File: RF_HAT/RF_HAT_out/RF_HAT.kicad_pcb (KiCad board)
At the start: 8 copper layers, 56 x 65 mm, 83 parts, among them J1 SMA, J2 SMA, J3 Raspberry_Pi_2_3, U1 CC1200RHBR, U2 CC1200RHBR, U3 RaspberryPi_Pico, Y1 40MHz, Y2 40MHz

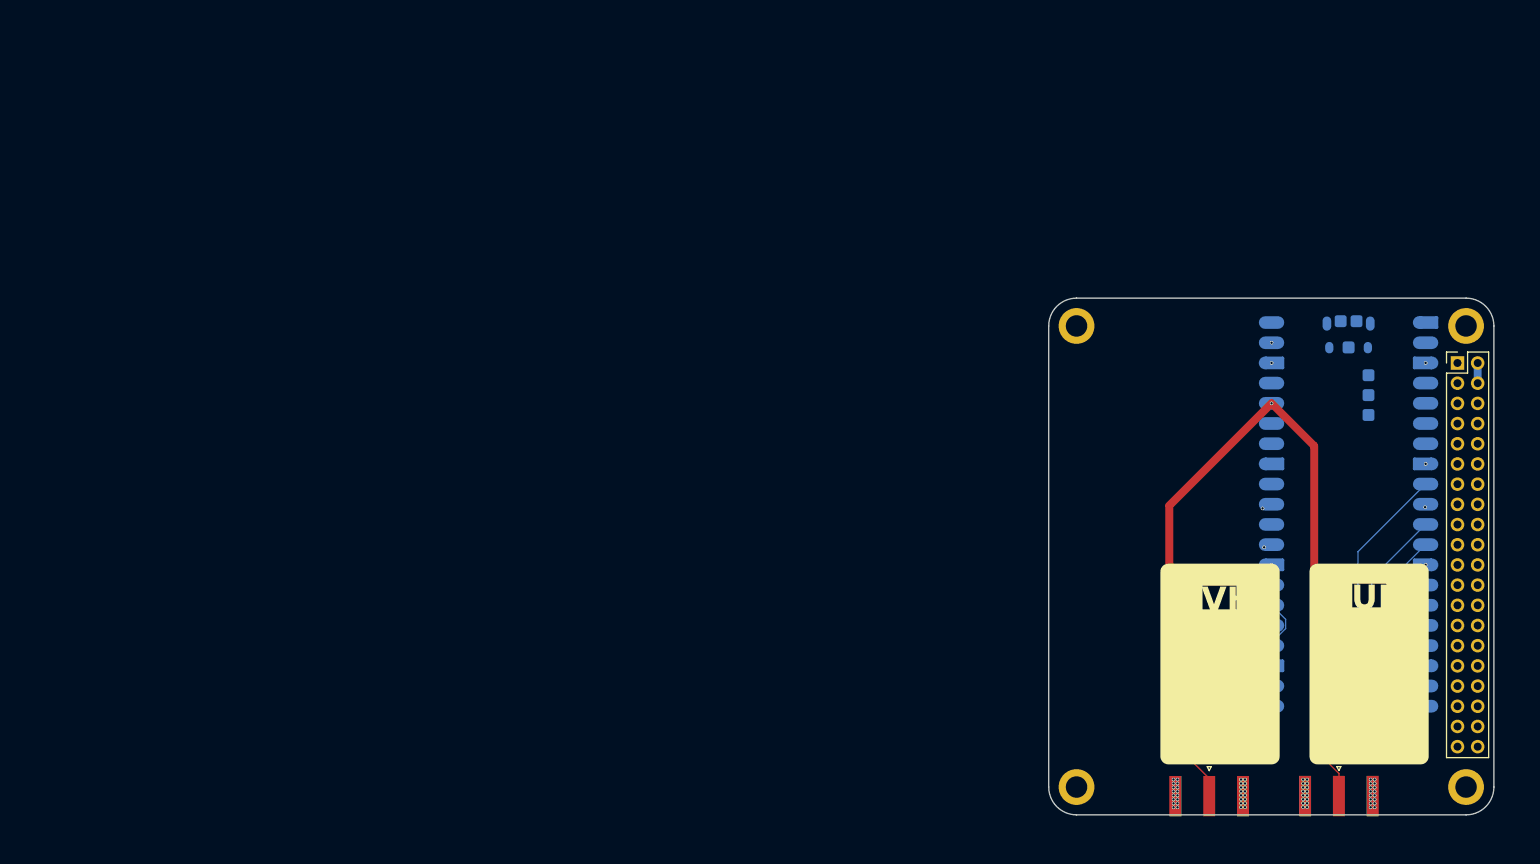
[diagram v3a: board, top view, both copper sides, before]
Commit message: Restructured kicad schematic for CC1200 PI_HAT readablitity based on M17 reference schematics
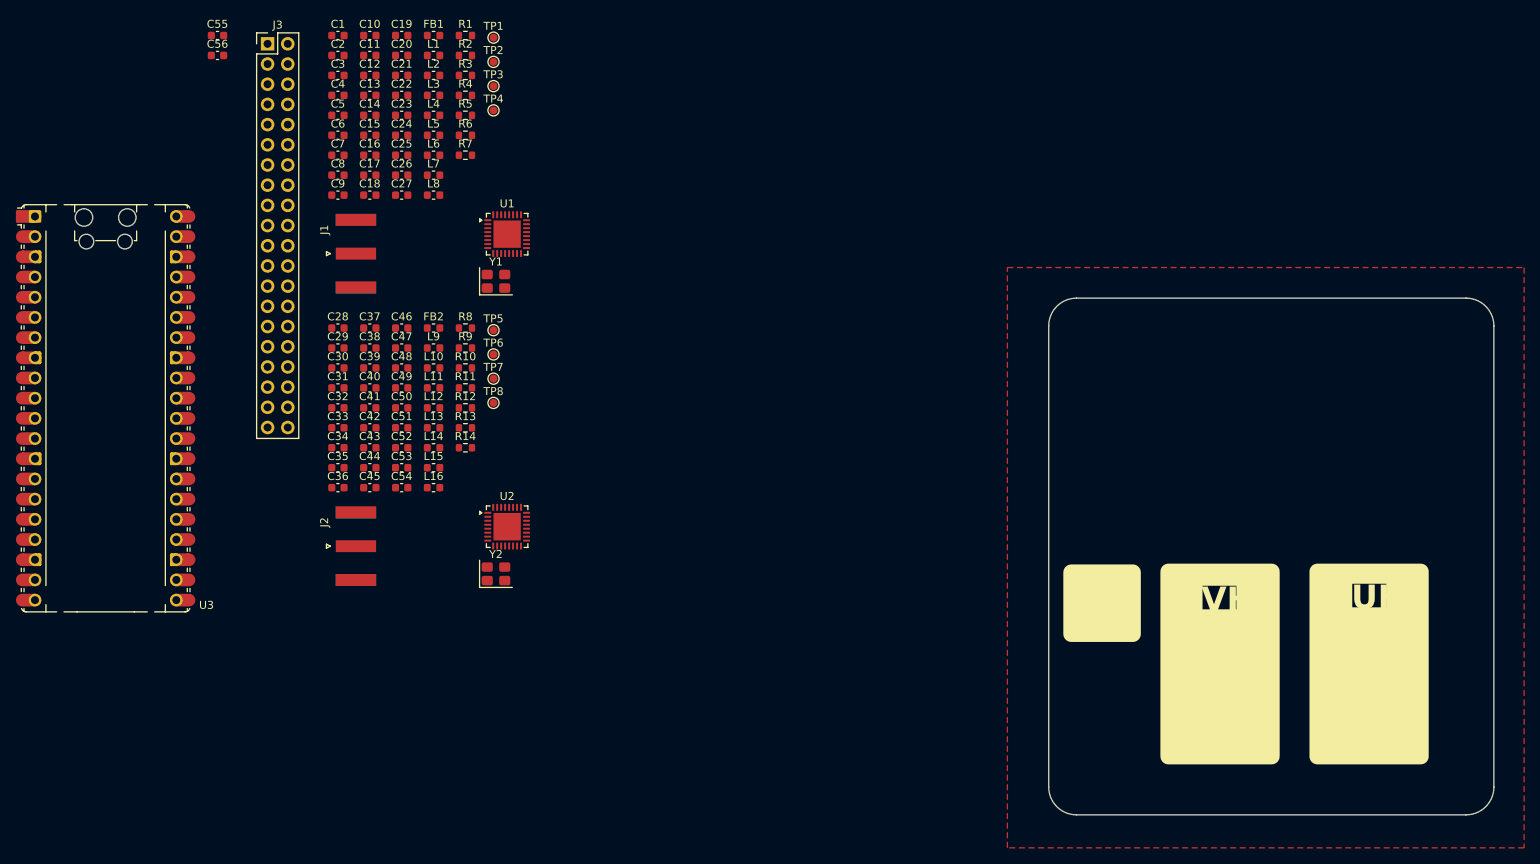
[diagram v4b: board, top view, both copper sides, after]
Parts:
- removed H1, H2, H3, H4: MountingHole_Pad, MountingHole:MountingHole_2.7mm_M2.5_ISO14580_Pad
- added C51: 47nF, Capacitor_SMD:C_0603_1608Metric, F.Cu at (80.8, 77.2)
- added C52: 47nF, Capacitor_SMD:C_0603_1608Metric, F.Cu at (80.8, 79.7)
- added C53: 47nF, Capacitor_SMD:C_0603_1608Metric, F.Cu at (80.8, 82.2)
- added C54: 47nF, Capacitor_SMD:C_0603_1608Metric, F.Cu at (80.8, 84.7)
- added C55: 100nF, Capacitor_SMD:C_0603_1608Metric, F.Cu at (57.6, 27.8)
- added C56: 100nF, Capacitor_SMD:C_0603_1608Metric, F.Cu at (57.6, 30.3)
- added L16: 100nH, Inductor_SMD:L_0603_1608Metric, F.Cu at (84.8, 84.7)
- added R10: 100R, Resistor_SMD:R_0603_1608Metric, F.Cu at (88.8, 69.6)
- added R11: 10k, Resistor_SMD:R_0603_1608Metric, F.Cu at (88.8, 72.1)
- added R12: 10k, Resistor_SMD:R_0603_1608Metric, F.Cu at (88.8, 74.7)
- added R13: 22R, Resistor_SMD:R_0603_1608Metric, F.Cu at (88.8, 77.2)
- added R14: 56k, Resistor_SMD:R_0603_1608Metric, F.Cu at (88.8, 79.7)
- added R5: 10k, Resistor_SMD:R_0603_1608Metric, F.Cu at (88.8, 37.9)
- added R6: 18R, Resistor_SMD:R_0603_1608Metric, F.Cu at (88.8, 40.4)
- added R7: 56k, Resistor_SMD:R_0603_1608Metric, F.Cu at (88.8, 42.9)
- added R8: 100R, Resistor_SMD:R_0603_1608Metric, F.Cu at (88.8, 64.6)
- added R9: 100R, Resistor_SMD:R_0603_1608Metric, F.Cu at (88.8, 67.1)
- added TP1: ~, TestPoint:TestPoint_Pad_D1.0mm, F.Cu at (92.4, 28.1)
- added TP2: ~, TestPoint:TestPoint_Pad_D1.0mm, F.Cu at (92.4, 31.1)
- added TP3: ~, TestPoint:TestPoint_Pad_D1.0mm, F.Cu at (92.4, 34.2)
- added TP4: ~, TestPoint:TestPoint_Pad_D1.0mm, F.Cu at (92.4, 37.2)
- added TP5: ~, TestPoint:TestPoint_Pad_D1.0mm, F.Cu at (92.4, 64.9)
- added TP6: ~, TestPoint:TestPoint_Pad_D1.0mm, F.Cu at (92.4, 67.9)
- added TP7: ~, TestPoint:TestPoint_Pad_D1.0mm, F.Cu at (92.4, 71.0)
- added TP8: ~, TestPoint:TestPoint_Pad_D1.0mm, F.Cu at (92.4, 74.0)
- C1: value 15pF -> 2.2pF
- C10: value 47nF -> 1nF
- C11, C38: value 47nF -> 10nF
- C12, C13, C35, C36, C39, C40: value 47nF -> 15pF
- C14, C15, C16, C41: value 47nF -> 100nF
- C17, C42: value 10nF -> 100nF
- C18: value 5.1pF -> 1.5nF
- C19: value 56pF -> 220nF
- C2: value 15pF -> 39pF
- C20: value 100pF -> 10nF
- C21: value 39pF -> 47nF
- C22, C25: value 5.1pF -> 47nF
- C23: value 6.2pF -> 47nF
- C24: value 2.2pF -> 47nF
- C26, C27, C48, C49: value 15pF -> 47nF
- C28: value 100nF -> 1.5pF
- C29: value 100nF -> 100pF
- C3: value 100nF -> 5.1pF
- C30, C31: value 100nF -> 15pF
- C32: value 1.8nF -> 100pF
- C33: value 220nF -> 10nF
- C34: value 10nF -> 100pF
- C37: value 47nF -> 100pF
- C4: value 100nF -> 6.2pF
- C43, C44: value 100pF -> 100nF
- C45: value 15pF -> 1.8nF
- C46: value 1.5pF -> 220nF
- C47: value 15pF -> 10nF
- C5: value 100nF -> 56pF
- C50: value 100pF -> 47nF
- C6: value 100nF -> 10nF
- C7: value 1.5nF -> 100pF
- C8: value 220nF -> 5.1pF
- C9: value 10nF -> 5.1pF
- L1: value 56nH -> 15nH
- L10: value 22nH -> 120nH
- L11: value 120nH -> 82nH
- L12: value 82nH -> 270nH
- L13: value 180nH -> 47nH
- L15: value 47nH -> 180nH
- L2: value 56nH -> 43nH
- L3: value 27nH -> 22nH
- L4: value 27nH -> 56nH
- L6: value 43nH -> 27nH
- L7: value 22nH -> 56nH
- L8: value 15nH -> 27nH
- L9: value 270nH -> 22nH
- R1, R3: value 56k -> 100R
- R2: value 18R -> 100R
- R4: value 22R -> 10k
- U3: footprint Module:RaspberryPi_Pico_SMD -> Module:RaspberryPi_Pico_Common_Unspecified; moved to F.Cu
- moved U3 156.9 mm to (43.6, 74.7), turned to 0 degrees
- moved C1 155.4 mm to (72.8, 27.8), turned to 0 degrees
- moved J3 155.0 mm to (63.9, 28.9)
- moved C10 153.9 mm to (76.8, 27.8)
- moved C5 153.1 mm to (72.8, 37.9)
- moved C19 151.8 mm to (80.8, 27.8), turned to 0 degrees
- moved C21 151.5 mm to (80.8, 32.8), turned to 0 degrees
- moved C20 151.5 mm to (80.8, 30.3)
- moved C2 150.5 mm to (72.8, 30.3)
- moved C6 150.0 mm to (72.8, 40.4)
- moved C4 149.4 mm to (72.8, 35.3), turned to 0 degrees
- moved C22 148.7 mm to (80.8, 35.3), turned to 0 degrees
- moved C7 148.6 mm to (72.8, 42.9), turned to 0 degrees
- moved C16 147.9 mm to (76.8, 42.9)
- moved C9 147.5 mm to (72.8, 47.9)
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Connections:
- C1 pad 1: /CC1200_UHF_432MHz/UHF_XOSC_Q1 -> /CC1200_UHF_432MHz/UHF_MN1
- C1 pad 2: /GND -> /CC1200_UHF_432MHz/UHF_MN2
- C10 pad 1: /CC1200_UHF_432MHz/UHF_AVDD_FILT -> /CC1200_UHF_432MHz/UHF_ANT_PRE
- C10 pad 2: /GND -> /CC1200_UHF_432MHz/UHF_ANT
- C12 pad 1: /CC1200_UHF_432MHz/UHF_AVDD_FILT -> /CC1200_UHF_432MHz/UHF_XOSC_Q1
- C13 pad 1: /CC1200_UHF_432MHz/UHF_AVDD_FILT -> /CC1200_UHF_432MHz/UHF_XOSC_Q2
- C14 pad 1: /CC1200_UHF_432MHz/UHF_AVDD_FILT -> /CC1200_UHF_432MHz/UHF_DCPL
- C15 pad 1: /CC1200_UHF_432MHz/UHF_AVDD_FILT -> /CC1200_UHF_432MHz/UHF_DCPL_VCO
- C16 pad 1: /CC1200_UHF_432MHz/UHF_AVDD_FILT -> /CC1200_UHF_432MHz/UHF_DCPL_PFD
- C17 pad 1: /CC1200_UHF_432MHz/UHF_AVDD_FILT -> /CC1200_UHF_432MHz/UHF_DCPL_XOSC
- C18 pad 1: /CC1200_UHF_432MHz/UHF_LN0 -> /CC1200_UHF_432MHz/UHF_LPF0
- C18 pad 2: /GND -> /CC1200_UHF_432MHz/UHF_LPF1
- C19 pad 1: /CC1200_UHF_432MHz/UHF_LN1 -> /CC1200_UHF_432MHz/UHF_AVDD_FILT
- C2 pad 1: /CC1200_UHF_432MHz/UHF_XOSC_Q2 -> /CC1200_UHF_432MHz/UHF_PA
- C2 pad 2: /GND -> /CC1200_UHF_432MHz/UHF_MN1
- C20 pad 1: /CC1200_UHF_432MHz/UHF_LN2 -> /CC1200_UHF_432MHz/UHF_AVDD_FILT
- C21 pad 1: /CC1200_UHF_432MHz/UHF_LN3 -> /CC1200_UHF_432MHz/UHF_AVDD_FILT
- C22 pad 1: /CC1200_UHF_432MHz/UHF_LN4 -> /CC1200_UHF_432MHz/UHF_AVDD_FILT
- C23 pad 1: /CC1200_UHF_432MHz/UHF_LN5 -> /CC1200_UHF_432MHz/UHF_AVDD_FILT
- C24 pad 1: /CC1200_UHF_432MHz/UHF_LN6 -> /CC1200_UHF_432MHz/UHF_AVDD_FILT
- C25 pad 1: /CC1200_UHF_432MHz/UHF_LN7 -> /CC1200_UHF_432MHz/UHF_AVDD_FILT
- C26 pad 1: /CC1200_VHF_144MHz/VHF_XOSC_Q1 -> /CC1200_UHF_432MHz/UHF_AVDD_FILT
- C27 pad 1: /CC1200_VHF_144MHz/VHF_XOSC_Q2 -> /CC1200_UHF_432MHz/UHF_AVDD_FILT
- C28 pad 1: /CC1200_VHF_144MHz/VHF_DCPL -> /CC1200_VHF_144MHz/VHF_MN1
- C28 pad 2: /GND -> /CC1200_VHF_144MHz/VHF_MN2
- C29 pad 1: /CC1200_VHF_144MHz/VHF_DCPL_VCO -> /CC1200_VHF_144MHz/VHF_PA
- C29 pad 2: /GND -> /CC1200_VHF_144MHz/VHF_MN1
- C3 pad 1: /CC1200_UHF_432MHz/UHF_DCPL -> /CC1200_UHF_432MHz/UHF_TRX
- C3 pad 2: /GND -> /CC1200_UHF_432MHz/UHF_MN2
- C30 pad 1: /CC1200_VHF_144MHz/VHF_DCPL_PFD -> /CC1200_VHF_144MHz/VHF_TRX
- C30 pad 2: /GND -> /CC1200_VHF_144MHz/VHF_MN2
- C31 pad 1: /CC1200_VHF_144MHz/VHF_DCPL_XOSC -> /CC1200_VHF_144MHz/VHF_MN3
- C32 pad 1: /CC1200_VHF_144MHz/VHF_LPF0 -> /CC1200_VHF_144MHz/VHF_PA_BIAS
- C32 pad 2: /CC1200_VHF_144MHz/VHF_LPF1 -> /CC1200_VHF_144MHz/VHF_AVDD_FILT
- C35 pad 1: /CC1200_VHF_144MHz/VHF_AVDD_FILT -> /CC1200_VHF_144MHz/VHF_BALUN
- C35 pad 2: /GND -> /CC1200_VHF_144MHz/VHF_LNA_P
- C36 pad 1: /CC1200_VHF_144MHz/VHF_AVDD_FILT -> /CC1200_VHF_144MHz/VHF_LNA_N
- C37 pad 1: /CC1200_VHF_144MHz/VHF_AVDD_FILT -> /CC1200_VHF_144MHz/VHF_ANT_PRE
- C37 pad 2: /GND -> /CC1200_VHF_144MHz/VHF_ANT
- C39 pad 1: /CC1200_VHF_144MHz/VHF_AVDD_FILT -> /CC1200_VHF_144MHz/VHF_XOSC_Q1
- C4 pad 1: /CC1200_UHF_432MHz/UHF_DCPL_VCO -> /CC1200_UHF_432MHz/UHF_MN3
- C40 pad 1: /CC1200_VHF_144MHz/VHF_AVDD_FILT -> /CC1200_VHF_144MHz/VHF_XOSC_Q2
- C41 pad 1: /CC1200_VHF_144MHz/VHF_AVDD_FILT -> /CC1200_VHF_144MHz/VHF_DCPL
- C42 pad 1: /CC1200_VHF_144MHz/VHF_AVDD_FILT -> /CC1200_VHF_144MHz/VHF_DCPL_VCO
- C43 pad 1: /CC1200_VHF_144MHz/VHF_LN0 -> /CC1200_VHF_144MHz/VHF_DCPL_PFD
- C44 pad 1: /CC1200_VHF_144MHz/VHF_LN1 -> /CC1200_VHF_144MHz/VHF_DCPL_XOSC
- C45 pad 1: /CC1200_VHF_144MHz/VHF_LN2 -> /CC1200_VHF_144MHz/VHF_LPF0
- C45 pad 2: /GND -> /CC1200_VHF_144MHz/VHF_LPF1
- C46 pad 1: /CC1200_VHF_144MHz/VHF_LN3 -> /CC1200_VHF_144MHz/VHF_AVDD_FILT
- C47 pad 1: /CC1200_VHF_144MHz/VHF_LN4 -> /CC1200_VHF_144MHz/VHF_AVDD_FILT
- C48 pad 1: /CC1200_VHF_144MHz/VHF_LN5 -> /CC1200_VHF_144MHz/VHF_AVDD_FILT
- C49 pad 1: /CC1200_VHF_144MHz/VHF_LN6 -> /CC1200_VHF_144MHz/VHF_AVDD_FILT
- C5 pad 1: /CC1200_UHF_432MHz/UHF_DCPL_PFD -> /CC1200_UHF_432MHz/UHF_PA_BIAS
- C5 pad 2: /GND -> /CC1200_UHF_432MHz/UHF_AVDD_FILT
- C50 pad 1: /CC1200_VHF_144MHz/VHF_LN6 -> /CC1200_VHF_144MHz/VHF_AVDD_FILT
- C6 pad 1: /CC1200_UHF_432MHz/UHF_DCPL_XOSC -> /CC1200_UHF_432MHz/UHF_AVDD_FILT
- C7 pad 1: /CC1200_UHF_432MHz/UHF_LPF0 -> /CC1200_UHF_432MHz/UHF_AVDD_FILT
- C7 pad 2: /CC1200_UHF_432MHz/UHF_LPF1 -> /GND
- C8 pad 1: /CC1200_UHF_432MHz/UHF_AVDD_FILT -> /CC1200_UHF_432MHz/UHF_BALUN
- C8 pad 2: /GND -> /CC1200_UHF_432MHz/UHF_LNA_P
- C9 pad 1: /CC1200_UHF_432MHz/UHF_AVDD_FILT -> /CC1200_UHF_432MHz/UHF_LNA_N
- J1 pad 1: /CC1200_UHF_432MHz/UHF_LN7 -> /CC1200_UHF_432MHz/UHF_ANT
- J2 pad 1: /CC1200_VHF_144MHz/VHF_LN6 -> /CC1200_VHF_144MHz/VHF_ANT
- L1 pad 2: /CC1200_UHF_432MHz/UHF_LN0 -> /CC1200_UHF_432MHz/UHF_MN2
- L10 pad 1: /CC1200_VHF_144MHz/VHF_LN0 -> /CC1200_VHF_144MHz/VHF_MN2
- L10 pad 2: /CC1200_VHF_144MHz/VHF_LN1 -> /CC1200_VHF_144MHz/VHF_MN3
- L11 pad 1: /CC1200_VHF_144MHz/VHF_LN1 -> /CC1200_VHF_144MHz/VHF_MN3
- L11 pad 2: /CC1200_VHF_144MHz/VHF_LN2 -> /CC1200_VHF_144MHz/VHF_ANT_PRE
- L12 pad 1: /CC1200_VHF_144MHz/VHF_LN2 -> /CC1200_VHF_144MHz/VHF_PA_BIAS
- L12 pad 2: /CC1200_VHF_144MHz/VHF_LN3 -> /CC1200_VHF_144MHz/VHF_PA
- L13 pad 1: /CC1200_VHF_144MHz/VHF_LN3 -> /CC1200_VHF_144MHz/VHF_BALUN
- L13 pad 2: /CC1200_VHF_144MHz/VHF_LN4 -> /CC1200_VHF_144MHz/VHF_TRX
- L14 pad 1: /CC1200_VHF_144MHz/VHF_LN4 -> /CC1200_VHF_144MHz/VHF_LNA_P
- L14 pad 2: /CC1200_VHF_144MHz/VHF_LN5 -> /GND
- L15 pad 1: /CC1200_VHF_144MHz/VHF_LN5 -> /CC1200_VHF_144MHz/VHF_LNA_P
- L15 pad 2: /CC1200_VHF_144MHz/VHF_LN6 -> /CC1200_VHF_144MHz/VHF_LNA_N
- L2 pad 1: /CC1200_UHF_432MHz/UHF_LN0 -> /CC1200_UHF_432MHz/UHF_MN2
- L2 pad 2: /CC1200_UHF_432MHz/UHF_LN1 -> /CC1200_UHF_432MHz/UHF_MN3
- L3 pad 1: /CC1200_UHF_432MHz/UHF_LN1 -> /CC1200_UHF_432MHz/UHF_MN3
- L3 pad 2: /CC1200_UHF_432MHz/UHF_LN2 -> /CC1200_UHF_432MHz/UHF_ANT_PRE
- L4 pad 1: /CC1200_UHF_432MHz/UHF_LN2 -> /CC1200_UHF_432MHz/UHF_PA_BIAS
- L4 pad 2: /CC1200_UHF_432MHz/UHF_LN3 -> /CC1200_UHF_432MHz/UHF_PA
- L5 pad 1: /CC1200_UHF_432MHz/UHF_LN3 -> /CC1200_UHF_432MHz/UHF_BALUN
- L5 pad 2: /CC1200_UHF_432MHz/UHF_LN4 -> /CC1200_UHF_432MHz/UHF_TRX
- L6 pad 1: /CC1200_UHF_432MHz/UHF_LN4 -> /CC1200_UHF_432MHz/UHF_LNA_P
- L6 pad 2: /CC1200_UHF_432MHz/UHF_LN5 -> /GND
- L7 pad 1: /CC1200_UHF_432MHz/UHF_LN5 -> /CC1200_UHF_432MHz/UHF_LNA_P
- L7 pad 2: /CC1200_UHF_432MHz/UHF_LN6 -> /CC1200_UHF_432MHz/UHF_LNA_N
- L8 pad 1: /CC1200_UHF_432MHz/UHF_LN6 -> /CC1200_UHF_432MHz/UHF_LNA_N
- L8 pad 2: /CC1200_UHF_432MHz/UHF_LN7 -> /CC1200_UHF_432MHz/UHF_BALUN
- L9 pad 2: /CC1200_VHF_144MHz/VHF_LN0 -> /CC1200_VHF_144MHz/VHF_MN2
- R1 pad 1: /CC1200_UHF_432MHz/UHF_RBIAS -> /UHF_SCLK
- R1 pad 2: /GND -> /CC1200_UHF_432MHz/UHF_SCLK_CC
- R2 pad 1: /CC1200_UHF_432MHz/UHF_PA -> /UHF_MOSI
- R2 pad 2: /CC1200_UHF_432MHz/UHF_MN1 -> /CC1200_UHF_432MHz/UHF_MOSI_CC
- R3 pad 1: /CC1200_VHF_144MHz/VHF_RBIAS -> /UHF_MISO
- R3 pad 2: /GND -> /CC1200_UHF_432MHz/UHF_MISO_CC
- R4 pad 1: /CC1200_VHF_144MHz/VHF_PA -> /+3.3V
- R4 pad 2: /CC1200_VHF_144MHz/VHF_MN1 -> /UHF_CSN
- U1 pad 12: /CC1200_UHF_432MHz/UHF_AVDD_FILT -> unconnected-(U1-DVDD-Pad12)
- U1 pad 18: /CC1200_UHF_432MHz/UHF_LN7 -> /CC1200_UHF_432MHz/UHF_TRX
- U1 pad 19: /CC1200_UHF_432MHz/UHF_LN7 -> /CC1200_UHF_432MHz/UHF_LNA_P
- U1 pad 20: /GND -> /CC1200_UHF_432MHz/UHF_LNA_N
- U1 pad 7: /UHF_MOSI -> /CC1200_UHF_432MHz/UHF_MOSI_CC
- U1 pad 8: /UHF_SCLK -> /CC1200_UHF_432MHz/UHF_SCLK_CC
- U1 pad 9: /UHF_MISO -> /CC1200_UHF_432MHz/UHF_MISO_CC
- U2 pad 12: /CC1200_VHF_144MHz/VHF_AVDD_FILT -> unconnected-(U2-DVDD-Pad12)
- U2 pad 18: /CC1200_VHF_144MHz/VHF_LN6 -> /CC1200_VHF_144MHz/VHF_TRX
- U2 pad 19: /CC1200_VHF_144MHz/VHF_LN6 -> /CC1200_VHF_144MHz/VHF_LNA_P
- U2 pad 20: /GND -> /CC1200_VHF_144MHz/VHF_LNA_N
- U2 pad 7: /VHF_MOSI -> /CC1200_VHF_144MHz/VHF_MOSI_CC
- U2 pad 8: /VHF_SCLK -> /CC1200_VHF_144MHz/VHF_SCLK_CC
- U2 pad 9: /VHF_MISO -> /CC1200_VHF_144MHz/VHF_MISO_CC
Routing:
- net /+3.3V: track 62.9 -> 0.00 mm, vias 1 -> 0
- net /GND: track 59.5 -> 0.00 mm, vias 169 -> 0
- net /CC1200_UHF_432MHz/UHF_AVDD_FILT: track 35.9 -> 0.00 mm, vias 9 -> 0
- net /CC1200_VHF_144MHz/VHF_AVDD_FILT: track 34.3 -> 0.00 mm, vias 11 -> 0
- net /UHF_GPIO3: track 24.3 -> 0.00 mm, vias 1 -> 0
- net /UHF_GPIO0: track 22.8 -> 0.00 mm, vias 2 -> 0
- net /VHF_GPIO3: track 22.3 -> 0.00 mm, vias 2 -> 0
- net /VHF_GPIO0: track 20.4 -> 0.00 mm, vias 2 -> 0
- net /CC1200_UHF_432MHz/UHF_LN7: track 18.7 -> 0.00 mm
- net /UHF_GPIO2: track 18.0 -> 0.00 mm, vias 1 -> 0
- net /CC1200_VHF_144MHz/VHF_LN6: track 17.8 -> 0.00 mm
- net /UHF_RESET: track 17.6 -> 0.00 mm, vias 1 -> 0
- net /VHF_MISO: track 14.8 -> 0.00 mm, vias 1 -> 0
- net /UHF_SCLK: track 14.4 -> 0.00 mm, vias 1 -> 0
- net /UHF_CSN: track 14.0 -> 0.00 mm, vias 2 -> 0
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- added copper zone on F.Cu, net /+5V

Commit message: added board edge and connector placement
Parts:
- removed C48, C49, C50, C51, C52, C53, C54: 47nF, Capacitor_SMD:C_0603_1608Metric
- removed C55, C56: 100nF, Capacitor_SMD:C_0603_1608Metric
- removed FB1, FB2: 1k@100MHz, Inductor_SMD:L_0603_1608Metric
- removed R10, R9: 100R, Resistor_SMD:R_0603_1608Metric
- removed R11, R12: 10k, Resistor_SMD:R_0603_1608Metric
- removed R13: 22R, Resistor_SMD:R_0603_1608Metric
- removed R14: 56k, Resistor_SMD:R_0603_1608Metric
- removed TP1, TP2, TP3, TP4, TP5, TP6, TP7, TP8: ~, TestPoint:TestPoint_Pad_D1.0mm
- added C57: 47nF, Capacitor_SMD:C_0603_1608Metric, F.Cu at (109.2, 95.2)
- added C58: 47nF, Capacitor_SMD:C_0603_1608Metric, F.Cu at (109.2, 97.7)
- added C59: 47nF, Capacitor_SMD:C_0603_1608Metric, F.Cu at (109.2, 100.2)
- added C60: 47nF, Capacitor_SMD:C_0603_1608Metric, F.Cu at (109.2, 102.7)
- added C61: 47nF, Capacitor_SMD:C_0603_1608Metric, F.Cu at (109.2, 105.2)
- added C62: 47nF, Capacitor_SMD:C_0603_1608Metric, F.Cu at (109.2, 107.7)
- added C63: 47nF, Capacitor_SMD:C_0603_1608Metric, F.Cu at (109.2, 110.2)
- added C64: 47nF, Capacitor_SMD:C_0603_1608Metric, F.Cu at (109.2, 112.7)
- added D1: D_Schottky, Diode_SMD:D_0603_1608Metric, F.Cu at (113.7, 134.2)
- added H1: MountingHole_Pad, MountingHole:MountingHole_2.7mm_M2.5_ISO7380_Pad, F.Cu at (214.7, 64.3)
- added H2: MountingHole_Pad, MountingHole:MountingHole_2.7mm_M2.5_ISO7380_Pad, F.Cu at (165.7, 64.3)
- added H3: MountingHole_Pad, MountingHole:MountingHole_2.7mm_M2.5_ISO7380_Pad, F.Cu at (165.7, 122.3)
- added H4: MountingHole_Pad, MountingHole:MountingHole_2.7mm_M2.5_ISO7380_Pad, F.Cu at (214.7, 122.3)
- added L18: XRTC303020D4R7MBCA, lib:IND-SMD_L3.0-W3.0_AFE303020S, F.Cu at (124.7, 128.3)
- added R16: 100k, Capacitor_SMD:C_0603_1608Metric, F.Cu at (124.6, 122.2)
- added R17: 13.7k, Capacitor_SMD:C_0603_1608Metric, F.Cu at (124.6, 124.8)
- added U4: XT30PW-M, Connector_AMASS:AMASS_XT30PW-M_1x02_P2.50mm_Horizontal, F.Cu at (117.4, 130.1)
- added U5: LMR51420YFDDCR, lib:SOT-23-6_L2.9-W1.6-P0.95-LS2.9-BL, F.Cu at (125.0, 132.8)
- C11, C20: value 10nF -> 15pF
- C14, C15, C42: value 100nF -> 47nF
- C16, C41: value 100nF -> 10nF
- C17: value 100nF -> 220nF
- C19: value 220nF -> 4.7uF 50v; footprint Capacitor_SMD:C_0603_1608Metric -> Capacitor_SMD:C_0805_2012Metric
- C22: value 47nF -> 100n
- C23: value 47nF -> 1.8nF
- C24: value 47nF -> 22uF
- C27: value 47nF -> 15pF
- C28: value 1.5pF -> 47nF
- C29, C37: value 100pF -> 47nF
- C30, C35, C36, C40: value 15pF -> 47nF
- C31: value 15pF -> 10nF
- C32: value 100pF -> 15pF
- C33: value 10nF -> 47nF
- C34: value 100pF -> 220nF
- C38, C47: value 10nF -> 100pF
- C39: value 15pF -> 100pF
- C43: value 100nF -> 100pF
- C44: value 100nF -> 1.5pF
- C45: value 1.8nF -> 15pF
- C46: value 220nF -> 15pF
- L10: value 120nH -> 100nH
- L11: value 82nH -> 47nH
- L12: value 270nH -> 100nH
- L13: value 47nH -> 270nH
- L14: value 100nH -> 22nH
- L15: value 180nH -> 120nH
- L16: value 100nH -> 82nH
- L9: value 22nH -> 100nH
- R1, R2: value 100R -> 10k
- R3: value 100R -> 56k
- R8: value 100R -> 22R
- U3: footprint Module:RaspberryPi_Pico_Common_Unspecified -> Module:RaspberryPi_Pico_SMD; moved to B.Cu
- moved U3 156.8 mm to (199.3, 92.6), turned to 180 degrees
- moved J3 154.8 mm to (213.4, 69.2)
- moved C19 110.4 mm to (109.5, 134.4)
- moved C22 92.9 mm to (124.6, 117.2)
- moved C24 90.6 mm to (124.6, 119.7)
- moved R2 72.7 mm to (96.3, 102.7)
- moved R1 72.7 mm to (96.3, 100.2)
- moved R3 72.7 mm to (96.3, 105.2)
- moved C20 67.3 mm to (80.3, 97.7)
- moved C11 64.9 mm to (80.3, 95.2)
- moved C23 62.3 mm to (80.3, 100.2)
- moved C25 59.8 mm to (80.3, 102.7)
- moved C26 59.8 mm to (80.3, 105.2)
- moved C27 59.8 mm to (80.3, 107.7)
- moved C37 48.7 mm to (84.3, 112.7)
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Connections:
- net /+5V renamed +5V
- net /CC1200_UHF_432MHz/UHF_ANT renamed Net-(J1-In)
- net /CC1200_UHF_432MHz/UHF_ANT_PRE renamed Net-(C10-Pad1)
- net /CC1200_UHF_432MHz/UHF_LNA_N renamed Net-(U1-LNA_N)
- net /CC1200_UHF_432MHz/UHF_MN1 renamed Net-(C1-Pad1)
- net /CC1200_UHF_432MHz/UHF_MN3 renamed Net-(C4-Pad1)
- net /CC1200_UHF_432MHz/UHF_PA renamed Net-(U1-PA)
- net /CC1200_UHF_432MHz/UHF_XOSC_Q1 renamed Net-(U1-XOSC_Q1)
- net /CC1200_UHF_432MHz/UHF_XOSC_Q2 renamed Net-(U1-XOSC_Q2)
- net /UART_RX renamed /Pi_Header/UART_RX
- net /UART_TX renamed /Pi_Header/UART_TX
- net /UHF_CSN renamed /CC1200_UHF_432MHz/UHF_CSN
- net /UHF_GPIO0 renamed /CC1200_UHF_432MHz/UHF_GPIO0
- net /UHF_GPIO2 renamed /CC1200_UHF_432MHz/UHF_GPIO2
- net /UHF_GPIO3 renamed /CC1200_UHF_432MHz/UHF_GPIO3
- net /UHF_RESET renamed /CC1200_UHF_432MHz/UHF_RESET
- C1 pad 2: /CC1200_UHF_432MHz/UHF_MN2 -> Net-(C1-Pad2)
- C11 pad 1: /CC1200_UHF_432MHz/UHF_AVDD_FILT -> Net-(U2-XOSC_Q1)
- C11 pad 2: /GND -> GND
- C12 pad 2: /GND -> GND
- C13 pad 2: /GND -> GND
- C14 pad 1: /CC1200_UHF_432MHz/UHF_DCPL -> Net-(U1-DCPL_PFD_CHP)
- C14 pad 2: /GND -> GND
- C15 pad 1: /CC1200_UHF_432MHz/UHF_DCPL_VCO -> Net-(U1-DCPL_XOSC)
- C15 pad 2: /GND -> GND
- C16 pad 1: /CC1200_UHF_432MHz/UHF_DCPL_PFD -> Net-(U1-DCPL_VCO)
- C16 pad 2: /GND -> GND
- C17 pad 1: /CC1200_UHF_432MHz/UHF_DCPL_XOSC -> Net-(U1-DCPL)
- C17 pad 2: /GND -> GND
- C18 pad 1: /CC1200_UHF_432MHz/UHF_LPF0 -> Net-(U1-LPF1)
- C18 pad 2: /CC1200_UHF_432MHz/UHF_LPF1 -> Net-(U1-LPF0)
- C19 pad 1: /CC1200_UHF_432MHz/UHF_AVDD_FILT -> +24V
- C19 pad 2: /GND -> GND
- C20 pad 1: /CC1200_UHF_432MHz/UHF_AVDD_FILT -> Net-(U2-XOSC_Q2)
- C20 pad 2: /GND -> GND
- C21 pad 1: /CC1200_UHF_432MHz/UHF_AVDD_FILT -> +3V3
- C21 pad 2: /GND -> GND
- C22 pad 1: /CC1200_UHF_432MHz/UHF_AVDD_FILT -> Net-(U5-SW)
- C22 pad 2: /GND -> Net-(U5-CB)
- C23 pad 1: /CC1200_UHF_432MHz/UHF_AVDD_FILT -> Net-(U2-LPF1)
- C23 pad 2: /GND -> Net-(U2-LPF0)
- C24 pad 1: /CC1200_UHF_432MHz/UHF_AVDD_FILT -> +5V_BUCK
- C24 pad 2: /GND -> GND
- C25 pad 1: /CC1200_UHF_432MHz/UHF_AVDD_FILT -> Net-(U2-DCPL_XOSC)
- C25 pad 2: /GND -> GND
- C26 pad 1: /CC1200_UHF_432MHz/UHF_AVDD_FILT -> +3V3
- C26 pad 2: /GND -> GND
- C27 pad 1: /CC1200_UHF_432MHz/UHF_AVDD_FILT -> Net-(U2-LNA_P)
- C27 pad 2: /GND -> Net-(C27-Pad2)
- C28 pad 1: /CC1200_VHF_144MHz/VHF_MN1 -> Net-(U2-DCPL_PFD_CHP)
- C28 pad 2: /CC1200_VHF_144MHz/VHF_MN2 -> GND
- C29 pad 1: /CC1200_VHF_144MHz/VHF_PA -> +3V3
- C29 pad 2: /CC1200_VHF_144MHz/VHF_MN1 -> GND
- C3 pad 1: /CC1200_UHF_432MHz/UHF_TRX -> Net-(C1-Pad2)
- C3 pad 2: /CC1200_UHF_432MHz/UHF_MN2 -> Net-(U1-TRX_SW)
- C30 pad 1: /CC1200_VHF_144MHz/VHF_TRX -> +3V3
- C30 pad 2: /CC1200_VHF_144MHz/VHF_MN2 -> GND
- C31 pad 1: /CC1200_VHF_144MHz/VHF_MN3 -> Net-(U2-DCPL_VCO)
- C31 pad 2: /GND -> GND
- C32 pad 1: /CC1200_VHF_144MHz/VHF_PA_BIAS -> Net-(U2-LNA_N)
- C32 pad 2: /CC1200_VHF_144MHz/VHF_AVDD_FILT -> GND
- C33 pad 1: /CC1200_VHF_144MHz/VHF_AVDD_FILT -> +3V3
- C33 pad 2: /GND -> GND
- C34 pad 1: /CC1200_VHF_144MHz/VHF_AVDD_FILT -> Net-(U2-DCPL)
- C34 pad 2: /GND -> GND
- C35 pad 1: /CC1200_VHF_144MHz/VHF_BALUN -> +3V3
- C35 pad 2: /CC1200_VHF_144MHz/VHF_LNA_P -> GND
- C36 pad 1: /CC1200_VHF_144MHz/VHF_LNA_N -> +3V3
- C36 pad 2: /GND -> GND
- C37 pad 1: /CC1200_VHF_144MHz/VHF_ANT_PRE -> +3V3
- C37 pad 2: /CC1200_VHF_144MHz/VHF_ANT -> GND
- C38 pad 1: /CC1200_VHF_144MHz/VHF_AVDD_FILT -> +3V3
- C38 pad 2: /GND -> Net-(C38-Pad2)
- C39 pad 1: /CC1200_VHF_144MHz/VHF_XOSC_Q1 -> Net-(U2-PA)
- C39 pad 2: /GND -> Net-(C39-Pad2)
- C4 pad 2: /GND -> GND
- C40 pad 1: /CC1200_VHF_144MHz/VHF_XOSC_Q2 -> +3V3
- C40 pad 2: /GND -> GND
- C41 pad 1: /CC1200_VHF_144MHz/VHF_DCPL -> +3V3
- C41 pad 2: /GND -> GND
- C42 pad 1: /CC1200_VHF_144MHz/VHF_DCPL_VCO -> +3V3
- C42 pad 2: /GND -> GND
- C43 pad 1: /CC1200_VHF_144MHz/VHF_DCPL_PFD -> +3V3
- C43 pad 2: /GND -> GND
- C44 pad 1: /CC1200_VHF_144MHz/VHF_DCPL_XOSC -> Net-(C39-Pad2)
- C44 pad 2: /GND -> Net-(C44-Pad2)
- C45 pad 1: /CC1200_VHF_144MHz/VHF_LPF0 -> Net-(C44-Pad2)
- C45 pad 2: /CC1200_VHF_144MHz/VHF_LPF1 -> Net-(U2-TRX_SW)
- C46 pad 1: /CC1200_VHF_144MHz/VHF_AVDD_FILT -> Net-(C46-Pad1)
- C46 pad 2: /GND -> GND
- C47 pad 1: /CC1200_VHF_144MHz/VHF_AVDD_FILT -> Net-(C47-Pad1)
- C47 pad 2: /GND -> Net-(J2-In)
- C5 pad 1: /CC1200_UHF_432MHz/UHF_PA_BIAS -> +3V3
- C5 pad 2: /CC1200_UHF_432MHz/UHF_AVDD_FILT -> Net-(C5-Pad2)
- C6 pad 1: /CC1200_UHF_432MHz/UHF_AVDD_FILT -> +3V3
- C6 pad 2: /GND -> GND
- C7 pad 1: /CC1200_UHF_432MHz/UHF_AVDD_FILT -> +3V3
- C7 pad 2: /GND -> GND
- C8 pad 1: /CC1200_UHF_432MHz/UHF_BALUN -> Net-(U1-LNA_P)
- C8 pad 2: /CC1200_UHF_432MHz/UHF_LNA_P -> Net-(C8-Pad2)
- C9 pad 2: /GND -> GND
- J1 pad 2: /GND -> GND
- J2 pad 1: /CC1200_VHF_144MHz/VHF_ANT -> Net-(J2-In)
- J2 pad 2: /GND -> GND
- J3 pad 1: /Pi_Header/VCC_3V3_PI -> unconnected-(J3-3V3-Pad1)
- J3 pad 14: /GND -> GND
- J3 pad 17: /Pi_Header/VCC_3V3_PI -> unconnected-(J3-3V3-Pad1)_1
- J3 pad 20: /GND -> GND
- J3 pad 25: /GND -> GND
- J3 pad 30: /GND -> GND
- J3 pad 34: /GND -> GND
- J3 pad 39: /GND -> GND
- J3 pad 6: /GND -> GND
- J3 pad 9: /GND -> GND
- L1 pad 2: /CC1200_UHF_432MHz/UHF_MN2 -> Net-(C1-Pad2)
- L10 pad 1: /CC1200_VHF_144MHz/VHF_MN2 -> Net-(U2-LNA_P)
- L10 pad 2: /CC1200_VHF_144MHz/VHF_MN3 -> Net-(U2-LNA_N)
- L11 pad 1: /CC1200_VHF_144MHz/VHF_MN3 -> Net-(C27-Pad2)
- L11 pad 2: /CC1200_VHF_144MHz/VHF_ANT_PRE -> Net-(U2-TRX_SW)
- L12 pad 1: /CC1200_VHF_144MHz/VHF_PA_BIAS -> Net-(U2-LNA_N)
- L12 pad 2: /CC1200_VHF_144MHz/VHF_PA -> Net-(C27-Pad2)
- L13 pad 1: /CC1200_VHF_144MHz/VHF_BALUN -> Net-(C38-Pad2)
- L13 pad 2: /CC1200_VHF_144MHz/VHF_TRX -> Net-(U2-PA)
- L14 pad 1: /CC1200_VHF_144MHz/VHF_LNA_P -> Net-(C39-Pad2)
- L14 pad 2: /GND -> Net-(C44-Pad2)
- L15 pad 1: /CC1200_VHF_144MHz/VHF_LNA_P -> Net-(C44-Pad2)
- L15 pad 2: /CC1200_VHF_144MHz/VHF_LNA_N -> Net-(C46-Pad1)
- L16 pad 1: /CC1200_VHF_144MHz/VHF_LNA_N -> Net-(C46-Pad1)
- L16 pad 2: /CC1200_VHF_144MHz/VHF_BALUN -> Net-(C47-Pad1)
- L2 pad 1: /CC1200_UHF_432MHz/UHF_MN2 -> Net-(C1-Pad2)
- L4 pad 1: /CC1200_UHF_432MHz/UHF_PA_BIAS -> Net-(C5-Pad2)
- L5 pad 1: /CC1200_UHF_432MHz/UHF_BALUN -> Net-(C8-Pad2)
- L5 pad 2: /CC1200_UHF_432MHz/UHF_TRX -> Net-(U1-TRX_SW)
- L6 pad 1: /CC1200_UHF_432MHz/UHF_LNA_P -> Net-(U1-LNA_P)
- L6 pad 2: /GND -> GND
- L7 pad 1: /CC1200_UHF_432MHz/UHF_LNA_P -> Net-(U1-LNA_P)
- L8 pad 2: /CC1200_UHF_432MHz/UHF_BALUN -> Net-(C8-Pad2)
- L9 pad 1: /CC1200_VHF_144MHz/VHF_MN1 -> Net-(U2-LNA_P)
- L9 pad 2: /CC1200_VHF_144MHz/VHF_MN2 -> GND
- R1 pad 1: /UHF_SCLK -> +3V3
- R1 pad 2: /CC1200_UHF_432MHz/UHF_SCLK_CC -> /CC1200_VHF_144MHz/UHF_CSN
- R2 pad 1: /UHF_MOSI -> +3V3
- R2 pad 2: /CC1200_UHF_432MHz/UHF_MOSI_CC -> /CC1200_VHF_144MHz/UHF_RESET
- R3 pad 1: /UHF_MISO -> GND
- R3 pad 2: /CC1200_UHF_432MHz/UHF_MISO_CC -> Net-(U2-RBIAS)
- R4 pad 1: /+3.3V -> +3V3
- R5 pad 1: /+3.3V -> +3V3
- R6 pad 1: /CC1200_UHF_432MHz/UHF_AVDD_FILT -> +3V3
- R6 pad 2: /CC1200_UHF_432MHz/UHF_PA_BIAS -> Net-(C5-Pad2)
- R7 pad 1: /CC1200_UHF_432MHz/UHF_RBIAS -> GND
- R7 pad 2: /GND -> Net-(U1-RBIAS)
- R8 pad 1: /VHF_SCLK -> +3V3
- R8 pad 2: /CC1200_VHF_144MHz/VHF_SCLK_CC -> Net-(C38-Pad2)
- U1 pad 1: /CC1200_UHF_432MHz/UHF_AVDD_FILT -> +3V3
- U1 pad 12: unconnected-(U1-DVDD-Pad12) -> +3V3
- U1 pad 13: /CC1200_UHF_432MHz/UHF_AVDD_FILT -> +3V3
- U1 pad 14: /CC1200_UHF_432MHz/UHF_RBIAS -> Net-(U1-RBIAS)
- U1 pad 15: /CC1200_UHF_432MHz/UHF_AVDD_FILT -> +3V3
- U1 pad 18: /CC1200_UHF_432MHz/UHF_TRX -> Net-(U1-TRX_SW)
- U1 pad 19: /CC1200_UHF_432MHz/UHF_LNA_P -> Net-(U1-LNA_P)
- U1 pad 21: /CC1200_UHF_432MHz/UHF_DCPL_VCO -> Net-(U1-DCPL_VCO)
- U1 pad 22: /CC1200_UHF_432MHz/UHF_AVDD_FILT -> +3V3
- U1 pad 23: /CC1200_UHF_432MHz/UHF_LPF0 -> Net-(U1-LPF0)
- U1 pad 24: /CC1200_UHF_432MHz/UHF_LPF1 -> Net-(U1-LPF1)
- U1 pad 25: /CC1200_UHF_432MHz/UHF_AVDD_FILT -> +3V3
- U1 pad 26: /CC1200_UHF_432MHz/UHF_DCPL_PFD -> Net-(U1-DCPL_PFD_CHP)
- U1 pad 27: /CC1200_UHF_432MHz/UHF_AVDD_FILT -> +3V3
- U1 pad 28: /CC1200_UHF_432MHz/UHF_AVDD_FILT -> +3V3
- U1 pad 29: /CC1200_UHF_432MHz/UHF_DCPL_XOSC -> Net-(U1-DCPL_XOSC)
- U1 pad 32: /GND -> GND
- U1 pad 33: /GND -> GND
- U1 pad 5: /CC1200_UHF_432MHz/UHF_AVDD_FILT -> +3V3
- U1 pad 6: /CC1200_UHF_432MHz/UHF_DCPL -> Net-(U1-DCPL)
- U1 pad 7: /CC1200_UHF_432MHz/UHF_MOSI_CC -> /CC1200_UHF_432MHz/UHF_MOSI
- U1 pad 8: /CC1200_UHF_432MHz/UHF_SCLK_CC -> /CC1200_UHF_432MHz/UHF_SCLK
- U1 pad 9: /CC1200_UHF_432MHz/UHF_MISO_CC -> /CC1200_UHF_432MHz/UHF_MISO
- U2 pad 1: /CC1200_VHF_144MHz/VHF_AVDD_FILT -> +3V3
- U2 pad 10: /VHF_GPIO0 -> /CC1200_VHF_144MHz/UHF_GPIO0
- U2 pad 11: /VHF_CSN -> /CC1200_VHF_144MHz/UHF_CSN
- U2 pad 12: unconnected-(U2-DVDD-Pad12) -> +3V3
- U2 pad 13: /CC1200_VHF_144MHz/VHF_AVDD_FILT -> +3V3
- U2 pad 14: /CC1200_VHF_144MHz/VHF_RBIAS -> Net-(U2-RBIAS)
- U2 pad 15: /CC1200_VHF_144MHz/VHF_AVDD_FILT -> +3V3
- U2 pad 17: /CC1200_VHF_144MHz/VHF_PA -> Net-(U2-PA)
- U2 pad 18: /CC1200_VHF_144MHz/VHF_TRX -> Net-(U2-TRX_SW)
- U2 pad 19: /CC1200_VHF_144MHz/VHF_LNA_P -> Net-(U2-LNA_P)
- U2 pad 2: /VHF_RESET -> /CC1200_VHF_144MHz/UHF_RESET
- U2 pad 20: /CC1200_VHF_144MHz/VHF_LNA_N -> Net-(U2-LNA_N)
- U2 pad 21: /CC1200_VHF_144MHz/VHF_DCPL_VCO -> Net-(U2-DCPL_VCO)
- U2 pad 22: /CC1200_VHF_144MHz/VHF_AVDD_FILT -> +3V3
- U2 pad 23: /CC1200_VHF_144MHz/VHF_LPF0 -> Net-(U2-LPF0)
- U2 pad 24: /CC1200_VHF_144MHz/VHF_LPF1 -> Net-(U2-LPF1)
- U2 pad 25: /CC1200_VHF_144MHz/VHF_AVDD_FILT -> +3V3
- U2 pad 26: /CC1200_VHF_144MHz/VHF_DCPL_PFD -> Net-(U2-DCPL_PFD_CHP)
- U2 pad 27: /CC1200_VHF_144MHz/VHF_AVDD_FILT -> +3V3
- U2 pad 28: /CC1200_VHF_144MHz/VHF_AVDD_FILT -> +3V3
- U2 pad 29: /CC1200_VHF_144MHz/VHF_DCPL_XOSC -> Net-(U2-DCPL_XOSC)
- U2 pad 3: /VHF_GPIO3 -> /CC1200_VHF_144MHz/UHF_GPIO3
- U2 pad 30: /CC1200_VHF_144MHz/VHF_XOSC_Q1 -> Net-(U2-XOSC_Q1)
- U2 pad 31: /CC1200_VHF_144MHz/VHF_XOSC_Q2 -> Net-(U2-XOSC_Q2)
- U2 pad 32: /GND -> GND
- U2 pad 33: /GND -> GND
- U2 pad 4: /VHF_GPIO2 -> /CC1200_VHF_144MHz/UHF_GPIO2
- U2 pad 5: /CC1200_VHF_144MHz/VHF_AVDD_FILT -> +3V3
- U2 pad 6: /CC1200_VHF_144MHz/VHF_DCPL -> Net-(U2-DCPL)
- U2 pad 7: /CC1200_VHF_144MHz/VHF_MOSI_CC -> /CC1200_VHF_144MHz/UHF_MOSI
- U2 pad 8: /CC1200_VHF_144MHz/VHF_SCLK_CC -> /CC1200_VHF_144MHz/UHF_SCLK
- U2 pad 9: /CC1200_VHF_144MHz/VHF_MISO_CC -> /CC1200_VHF_144MHz/UHF_MISO
- U3 pad 13: /GND -> GND
- U3 pad 14: /UHF_SCLK -> /CC1200_UHF_432MHz/UHF_SCLK
- U3 pad 15: /UHF_MOSI -> /CC1200_UHF_432MHz/UHF_MOSI
- U3 pad 16: /UHF_MISO -> /CC1200_UHF_432MHz/UHF_MISO
- U3 pad 18: /GND -> GND
- U3 pad 21: /VHF_MISO -> /Pico_SPI_Host/VHF_MISO
- U3 pad 22: /VHF_CSN -> /Pico_SPI_Host/VHF_CSN
- U3 pad 23: /GND -> GND
- U3 pad 24: /VHF_SCLK -> /Pico_SPI_Host/VHF_SCLK
- U3 pad 25: /VHF_MOSI -> /Pico_SPI_Host/VHF_MOSI
- U3 pad 26: /VHF_RESET -> /Pico_SPI_Host/VHF_RESET
- U3 pad 27: /VHF_GPIO2 -> /Pico_SPI_Host/VHF_GPIO2
- U3 pad 28: /GND -> GND
- U3 pad 29: /VHF_GPIO0 -> /Pico_SPI_Host/VHF_GPIO0
- U3 pad 3: /GND -> GND
- U3 pad 31: /VHF_GPIO3 -> /Pico_SPI_Host/VHF_GPIO3
- U3 pad 33: unconnected-(U3-AGND-Pad33) -> GND
- U3 pad 36: /+3.3V -> +3V3
- U3 pad 38: /GND -> GND
- U3 pad 40: unconnected-(U3-VBUS-Pad40) -> +5V_USB
- U3 pad 8: /GND -> GND
- Y1 pad 2: /GND -> GND
- Y1 pad 4: /GND -> GND
- Y2 pad 1: /CC1200_VHF_144MHz/VHF_XOSC_Q1 -> Net-(U2-XOSC_Q1)
- Y2 pad 2: /GND -> GND
- Y2 pad 3: /CC1200_VHF_144MHz/VHF_XOSC_Q2 -> Net-(U2-XOSC_Q2)
- Y2 pad 4: /GND -> GND
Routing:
- added copper zone on In4.Cu, net (none)
- added copper zone on In4.Cu, net +3V3
- added copper zone on In1.Cu, net GND
- added copper zone on In3.Cu, net GND
- added copper zone on In5.Cu, net GND
- added copper zone on In6.Cu, net GND
- removed copper zone on In4.Cu, net /CC1200_UHF_432MHz/UHF_AVDD_FILT
- removed copper zone on In4.Cu, net /CC1200_VHF_144MHz/VHF_AVDD_FILT
- removed copper zone on In1.Cu, net /GND
- removed copper zone on In3.Cu, net /GND
- removed copper zone on In5.Cu, net /GND
- removed copper zone on In6.Cu, net /GND
